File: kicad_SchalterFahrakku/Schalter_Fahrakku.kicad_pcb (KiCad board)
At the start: 2 copper layers, 15 parts, among them P1 V+_IN, P2 V-_IN, P3 V+_OUT, P4 V-_OUT, Q1 IRLML6344, Q2 IPD90P03

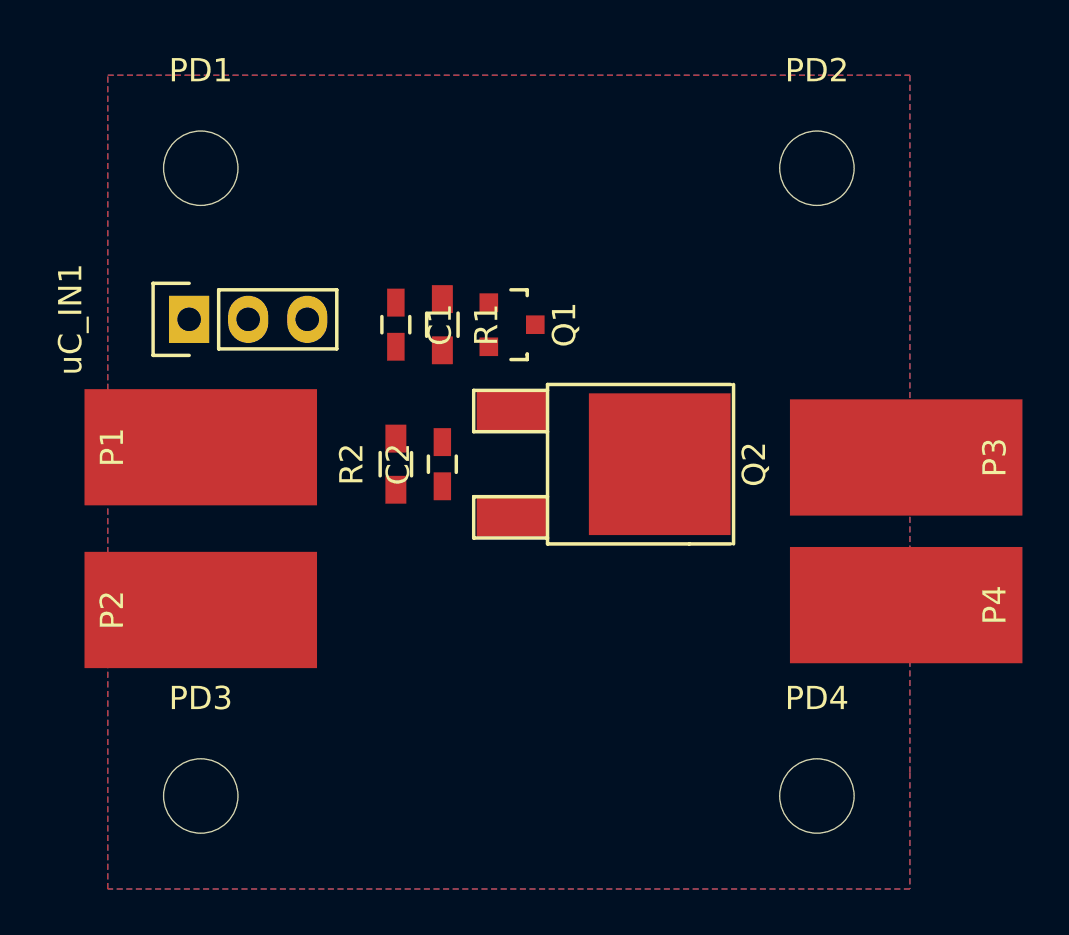
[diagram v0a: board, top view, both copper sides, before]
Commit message: - Neue anschlüsse in Schalterplatine eingefügt
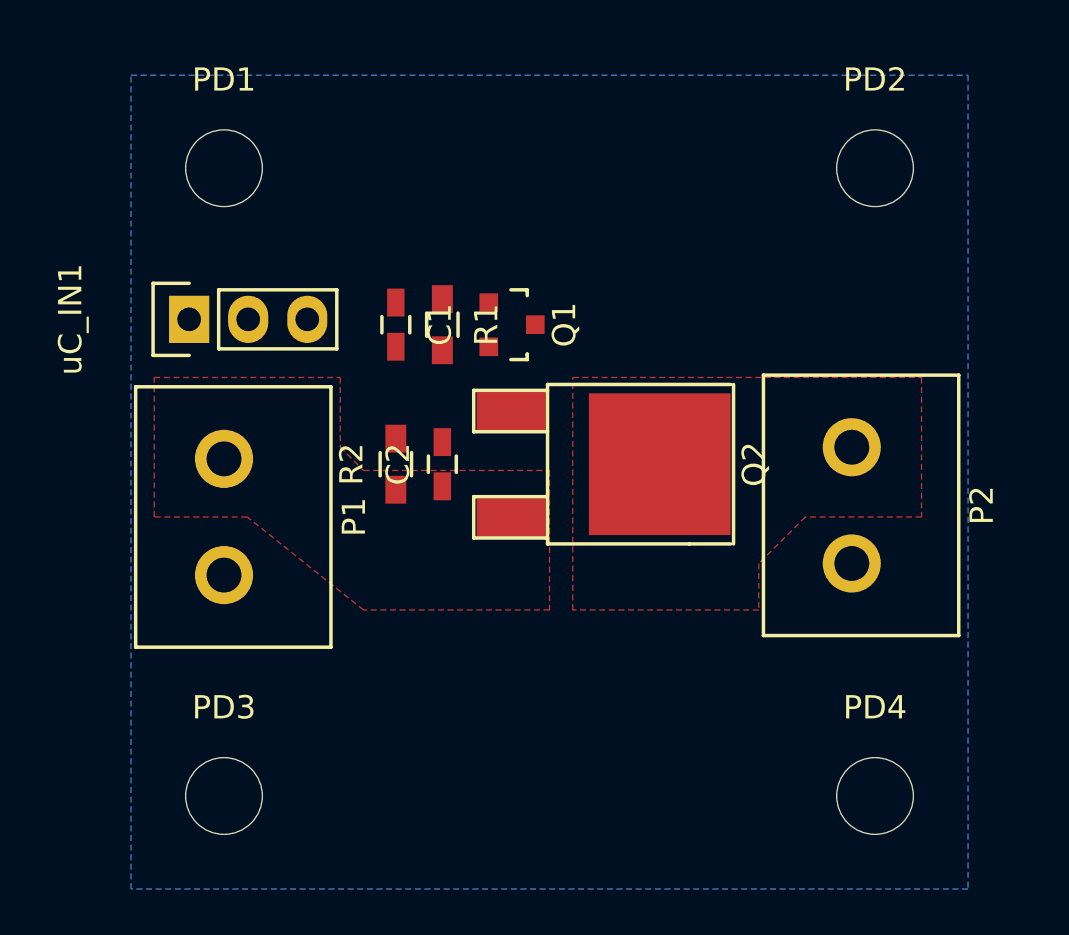
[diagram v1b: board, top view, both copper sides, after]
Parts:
- removed P3: V+_OUT, Wire_Pads:SolderWirePad_single_SMD_5x10mm
- removed P4: V-_OUT, Wire_Pads:SolderWirePad_single_SMD_5x10mm
- P1: value V+_IN -> V_IN; footprint Wire_Pads:SolderWirePad_single_SMD_5x10mm -> Custom:AKL_320-02
- P2: value V-_IN -> V_OUT; footprint Wire_Pads:SolderWirePad_single_SMD_5x10mm -> Custom:AKL_320-02
- PD1, PD2, PD3, PD4: footprint Mounting_Holes:MountingHole_3.2mm_M3 -> Custom:MountingHole_3.3mm_M3
- moved P2 28.9 mm to (178.0, 91.0), turned to 270 degrees
- moved PD2 2.50 mm to (179.0, 79.0)
- moved PD4 2.50 mm to (179.0, 106.0)
- moved P1 1.12 mm to (151.0, 91.5), turned to 270 degrees
- moved PD1 1.00 mm to (151.0, 79.0)
- moved PD3 1.00 mm to (151.0, 106.0)
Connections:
- P2 pad 1: GND -> Net-(P2-Pad1)
- Q2 pad 2: Net-(P3-Pad1) -> Net-(P2-Pad1)
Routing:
- added copper zone on F.Cu, net Net-(C2-Pad1)
- added copper zone on F.Cu, net Net-(P2-Pad1)
- removed copper zone on F.Cu, net GND

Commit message: - RC-Glieder an ADC hinzugefügt - Wannenstecker mit Spannungsversorgung an Op-Amps hinzugefügt - 0R Widerstände an Op-Amp Ausgängen hinzugefügt
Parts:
- moved P2 5.10 mm to (179.0, 96.0), turned to 90 degrees
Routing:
- added copper zone on F.Cu, net GND
- removed copper zone on F.Cu, net Net-(P2-Pad1)
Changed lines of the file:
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@@
     (links 16)
     (no_connects 16)
-    (area 143.275 74.075 184.375 110.775)
+    (area 143.275 74.075 184.575 110.775)
     (thickness 1.6)
     (drawings 4)
@@
   )
   (module Custom:AKL_320-02 (layer F.Cu)
-    (at 178 91 270)
-    (fp_text reference P2 (at 2.5 -5.6 270) (layer F.SilkS)
-      (effects (font (size 1 1) (thickness 0.15)))
-    )
-    (fp_text value V_OUT (at 2.5 4.8 270) (layer F.Fab)
+    (at 179 96 90)
+    (fp_text reference P2 (at 2.5 -5.6 90) (layer F.SilkS)
+      (effects (font (size 1 1) (thickness 0.15)))
+    )
+    (fp_text value V_OUT (at 2.5 4.8 90) (layer F.Fab)
       (effects (font (size 1 1) (thickness 0.15)))
     )
@@
     (fp_line (start -3.1 -4.6) (end 8.1 -4.6) (layer F.SilkS) (width 0.15))
     (fp_line (start -3.1 3.8) (end 8.1 3.8) (layer F.SilkS) (width 0.15))
-    (pad 2 thru_hole circle (at 5 0 270) (size 2.5 2.5) (drill 1.5) (layers *.Cu *.Mask F.SilkS)
-      (net 2 GND))
-    (pad 1 thru_hole circle (at 0 0 270) (size 2.5 2.5) (drill 1.5) (layers *.Cu *.Mask F.SilkS)
+    (pad 2 thru_hole circle (at 5 0 90) (size 2.5 2.5) (drill 1.5) (layers *.Cu *.Mask F.SilkS)
+      (net 2 GND))
+    (pad 1 thru_hole circle (at 0 0 90) (size 2.5 2.5) (drill 1.5) (layers *.Cu *.Mask F.SilkS)
       (net 5 "Net-(P2-Pad1)"))
   )
@@
   (gr_line (start 183 110) (end 183 75) (angle 90) (layer Margin) (width 0.2))
   (gr_line (start 147 110) (end 183 110) (angle 90) (layer Margin) (width 0.2))
-  (zone (net 3) (net_name "Net-(C2-Pad1)") (layer F.Cu) (hatch edge 0.508)
-    (connect_pads (clearance 0.508))
-    (min_thickness 0.254)
-    (fill yes (arc_segments 16) (thermal_gap 0.508) (thermal_bridge_width 0.508))
-    (polygon
-      (pts
-        (xy 156 91) (xy 157 92) (xy 165 92) (xy 165 98) (xy 157 98)
-        (xy 152 94) (xy 148 94) (xy 148 88) (xy 156 88) (xy 156 91)
-      )
-    )
-  )
-  (zone (net 5) (net_name "Net-(P2-Pad1)") (layer F.Cu) (hatch edge 0.508)
-    (connect_pads (clearance 0.508))
-    (min_thickness 0.254)
-    (fill yes (arc_segments 16) (thermal_gap 0.508) (thermal_bridge_width 0.508))
-    (polygon
-      (pts
-        (xy 181 94) (xy 176 94) (xy 174 96) (xy 174 98) (xy 166 98)
-        (xy 166 88) (xy 181 88) (xy 181 94)
-      )
-    )
-  )
   (zone (net 2) (net_name GND) (layer B.Cu) (hatch edge 0.508)
     (connect_pads (clearance 0.508))
@@
       )
     )
+  )
+  (zone (net 2) (net_name GND) (layer F.Cu) (hatch edge 0.508)
+    (connect_pads (clearance 0.508))
+    (min_thickness 0.254)
+    (fill (arc_segments 16) (thermal_gap 0.508) (thermal_bridge_width 0.508))
+    (polygon
+      (pts
+        (xy 183 110) (xy 147 110) (xy 147 75) (xy 183 75) (xy 183 110)
+      )
+    )
+    (polygon
+      (pts        (xy 165.75 87.5) (xy 165.75 91.5) (xy 156.75 91.5) (xy 154.75 89) (xy 148.5 89)
+        (xy 148.5 94) (xy 153.5 94) (xy 155.25 96) (xy 172.5 96) (xy 175 98.5)
+        (xy 181.5 98.5) (xy 181.5 93.5) (xy 176.5 93.5) (xy 174.25 91) (xy 174.25 87.5)
+        (xy 165.75 87.5)
+      )
+    )
+  )
+  (zone (net 3) (net_name "Net-(C2-Pad1)") (layer F.Cu) (hatch edge 0.508)
+    (connect_pads (clearance 0.508))
+    (min_thickness 0.254)
+    (fill (arc_segments 16) (thermal_gap 0.508) (thermal_bridge_width 0.508))
+    (polygon
+      (pts
+        (xy 156.5 92.5) (xy 165 92.5) (xy 165 95.25) (xy 155.75 95.25) (xy 154 93.25)
+        (xy 149.25 93.25) (xy 149.25 89.75) (xy 154.25 89.75)
+      )
+    )
+    (polygon
+      (pts        (xy 149.25 89.75)
+      )
+    )

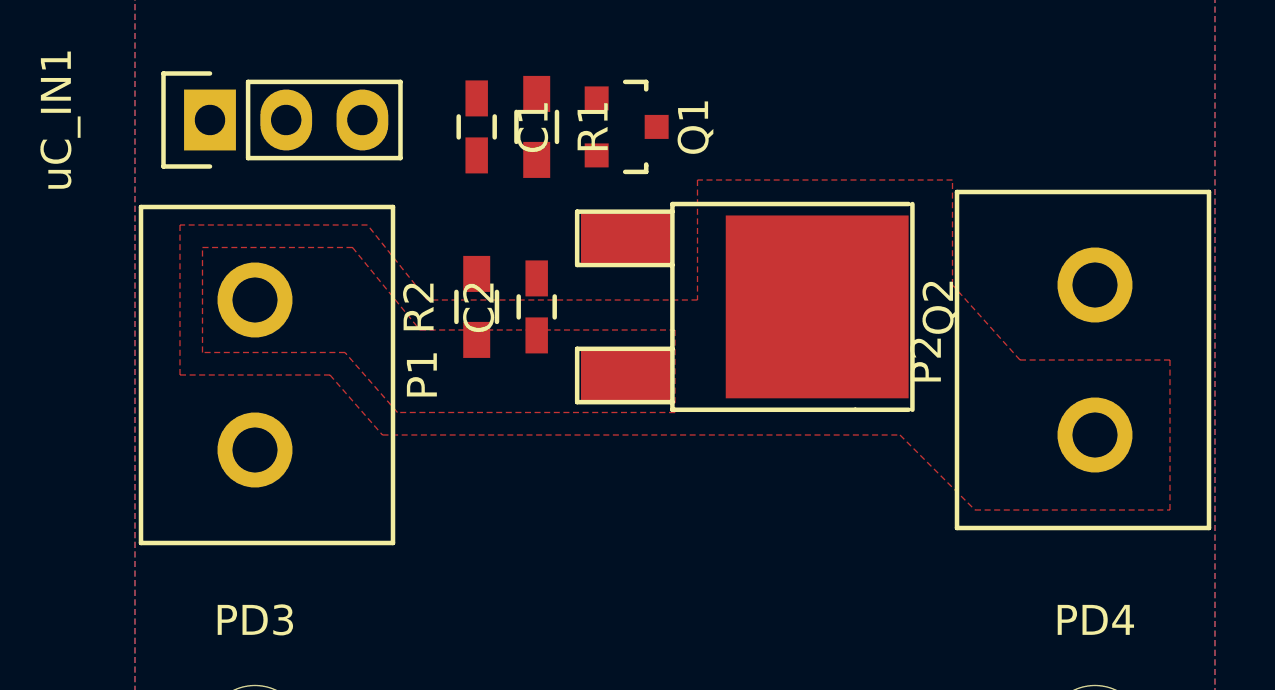
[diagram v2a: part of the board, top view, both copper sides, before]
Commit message: - Schaltplan uCSensorik finalisiert (1 pin an uC Frei geworden) - ERC wirft 8 Warnungen, keine Fehler
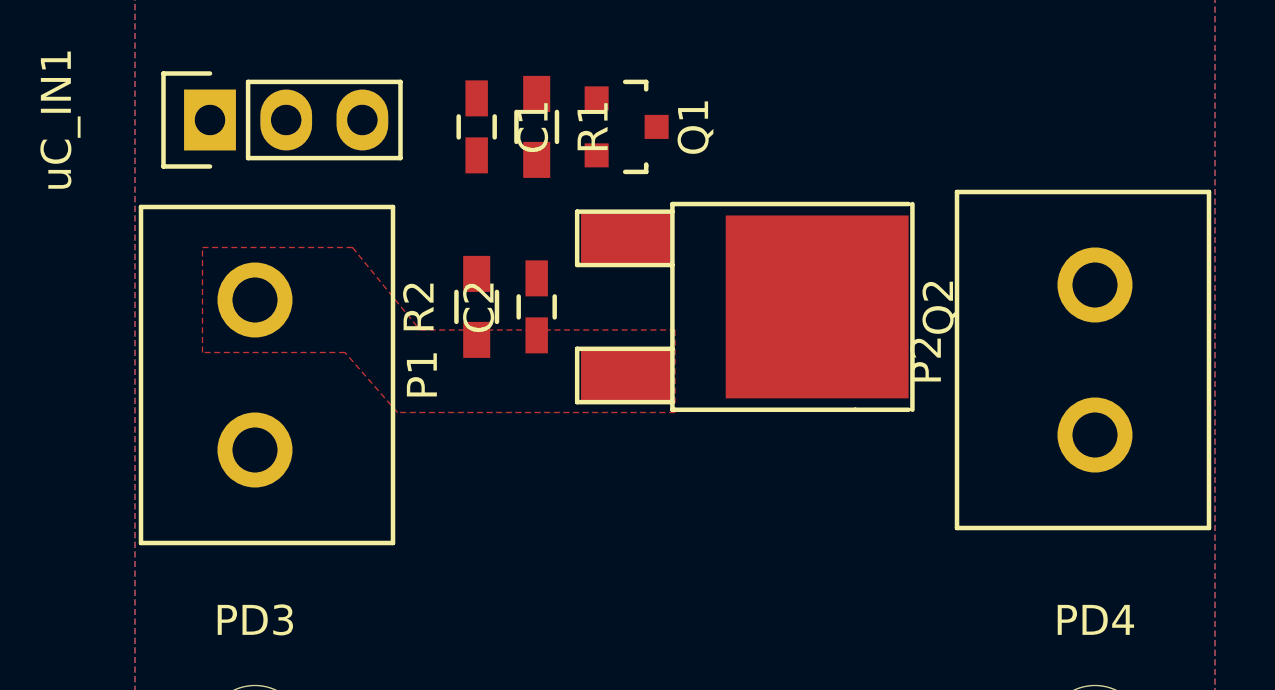
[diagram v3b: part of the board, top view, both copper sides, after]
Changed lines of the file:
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@@
   (general
     (links 16)
-    (no_connects 16)
-    (area 143.275 74.075 184.575 110.775)
+    (no_connects 8)
+    (area 143.275 74.075 184.775 110.775)
     (thickness 1.6)
     (drawings 4)
@@
     (connect_pads (clearance 0.508))
     (min_thickness 0.254)
-    (fill (arc_segments 16) (thermal_gap 0.508) (thermal_bridge_width 0.508))
+    (fill yes (arc_segments 16) (thermal_gap 0.508) (thermal_bridge_width 0.508))
     (polygon
       (pts
@@
     (connect_pads (clearance 0.508))
     (min_thickness 0.254)
-    (fill (arc_segments 16) (thermal_gap 0.508) (thermal_bridge_width 0.508))
+    (fill yes (arc_segments 16) (thermal_gap 0.508) (thermal_bridge_width 0.508))
     (polygon
       (pts
@@
       )
     )
-    (polygon
-      (pts        (xy 165.75 87.5) (xy 165.75 91.5) (xy 156.75 91.5) (xy 154.75 89) (xy 148.5 89)
-        (xy 148.5 94) (xy 153.5 94) (xy 155.25 96) (xy 172.5 96) (xy 175 98.5)
-        (xy 181.5 98.5) (xy 181.5 93.5) (xy 176.5 93.5) (xy 174.25 91) (xy 174.25 87.5)
-        (xy 165.75 87.5)
-      )
-    )
   )
   (zone (net 3) (net_name "Net-(C2-Pad1)") (layer F.Cu) (hatch edge 0.508)
+    (priority 1)
     (connect_pads (clearance 0.508))
     (min_thickness 0.254)
-    (fill (arc_segments 16) (thermal_gap 0.508) (thermal_bridge_width 0.508))
+    (fill yes (arc_segments 16) (thermal_gap 0.508) (thermal_bridge_width 0.508))
     (polygon
       (pts

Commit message: - Layout Grob sortiert - Fehler an CAR-ID DIP behoben(Pin Zuordnung Fehlerhaft) - Fehler an GNDD behoben (GNDA und GNDD vertauscht an TEN30)
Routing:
- removed copper zone on F.Cu, net Net-(C2-Pad1)
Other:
- net class Default: via_drill 0.4 -> 0.2
- rule via_min_drill: 0.3 -> 0.2
- rule via_min_size: 0.4 -> 0.6
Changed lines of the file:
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@@
   (setup
     (last_trace_width 0.25)
+    (user_trace_width 0.2)
+    (user_trace_width 0.25)
+    (user_trace_width 0.3)
+    (user_trace_width 0.5)
+    (user_trace_width 0.8)
+    (user_trace_width 1)
+    (user_trace_width 2)
     (trace_clearance 0.2)
     (zone_clearance 0.508)
@@
     (edge_width 0.15)
     (via_size 0.6)
-    (via_drill 0.4)
-    (via_min_size 0.4)
-    (via_min_drill 0.3)
+    (via_drill 0.2)
+    (via_min_size 0.6)
+    (via_min_drill 0.2)
+    (user_via 0.6 0.2)
+    (user_via 1.2 0.8)
+    (user_via 1.4 1)
+    (user_via 9 0.5)
     (uvia_size 0.3)
     (uvia_drill 0.1)
@@
     (trace_width 0.25)
     (via_dia 0.6)
-    (via_drill 0.4)
+    (via_drill 0.2)
     (uvia_dia 0.3)
     (uvia_drill 0.1)
@@
       )
     )
-  )
-  (zone (net 3) (net_name "Net-(C2-Pad1)") (layer F.Cu) (hatch edge 0.508)
-    (priority 1)
-    (connect_pads (clearance 0.508))
-    (min_thickness 0.254)
-    (fill yes (arc_segments 16) (thermal_gap 0.508) (thermal_bridge_width 0.508))
-    (polygon
-      (pts
-        (xy 156.5 92.5) (xy 165 92.5) (xy 165 95.25) (xy 155.75 95.25) (xy 154 93.25)
-        (xy 149.25 93.25) (xy 149.25 89.75) (xy 154.25 89.75)
-      )
-    )
-    (polygon
-      (pts        (xy 149.25 89.75)
-      )
-    )

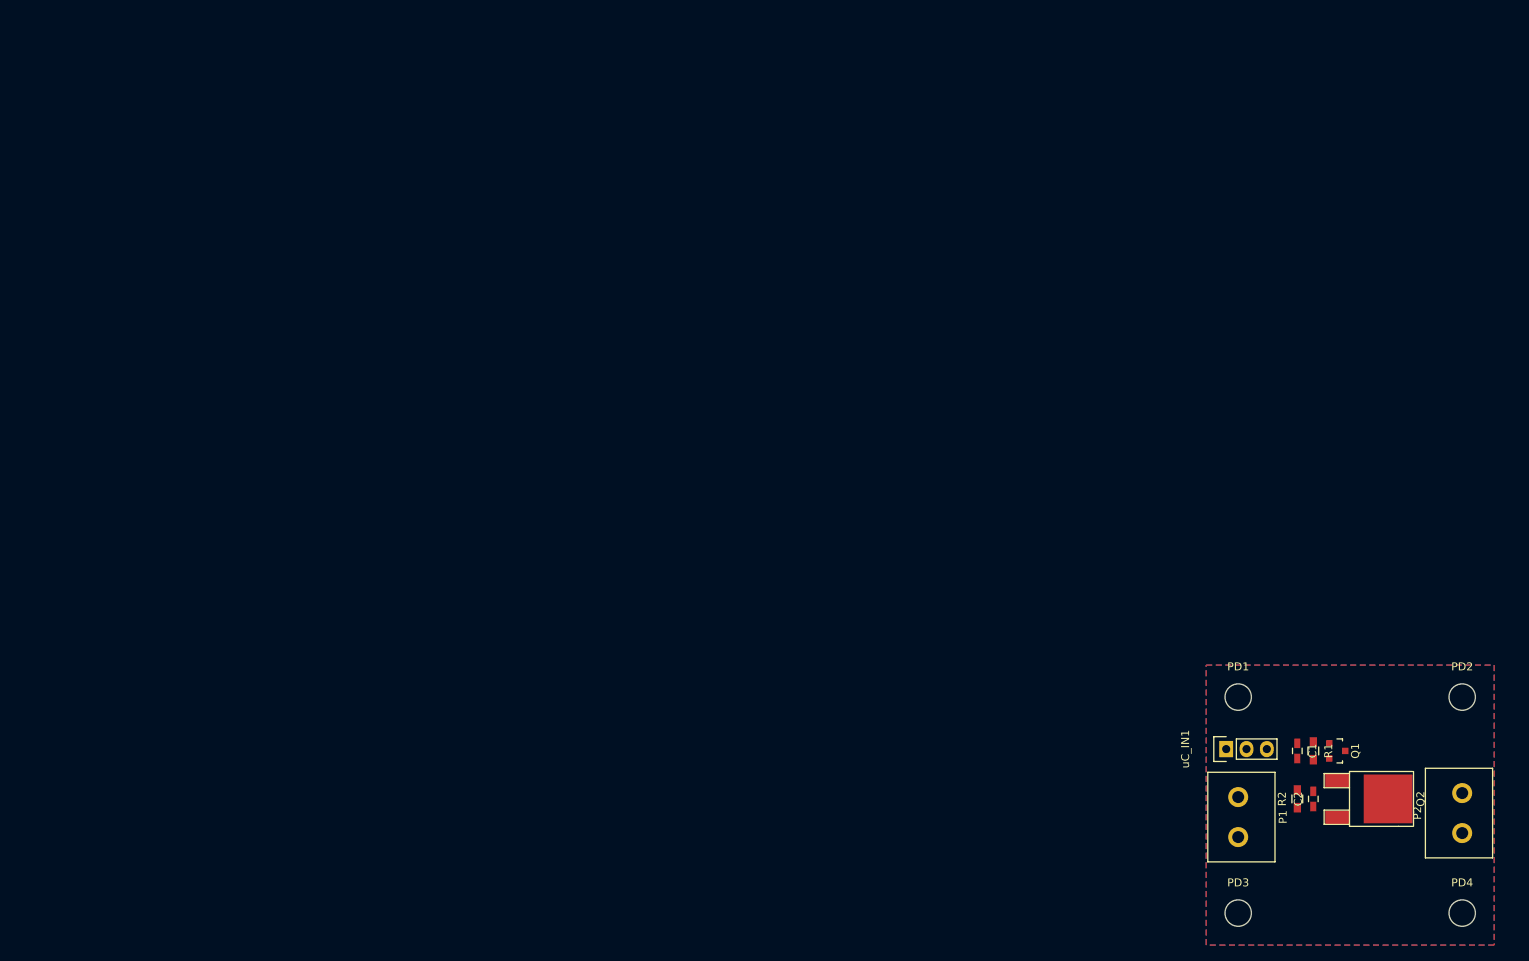
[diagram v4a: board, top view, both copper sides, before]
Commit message: - RC-Glieder im Schaltplan hinzugefügt - LED4 Hinzugefügt
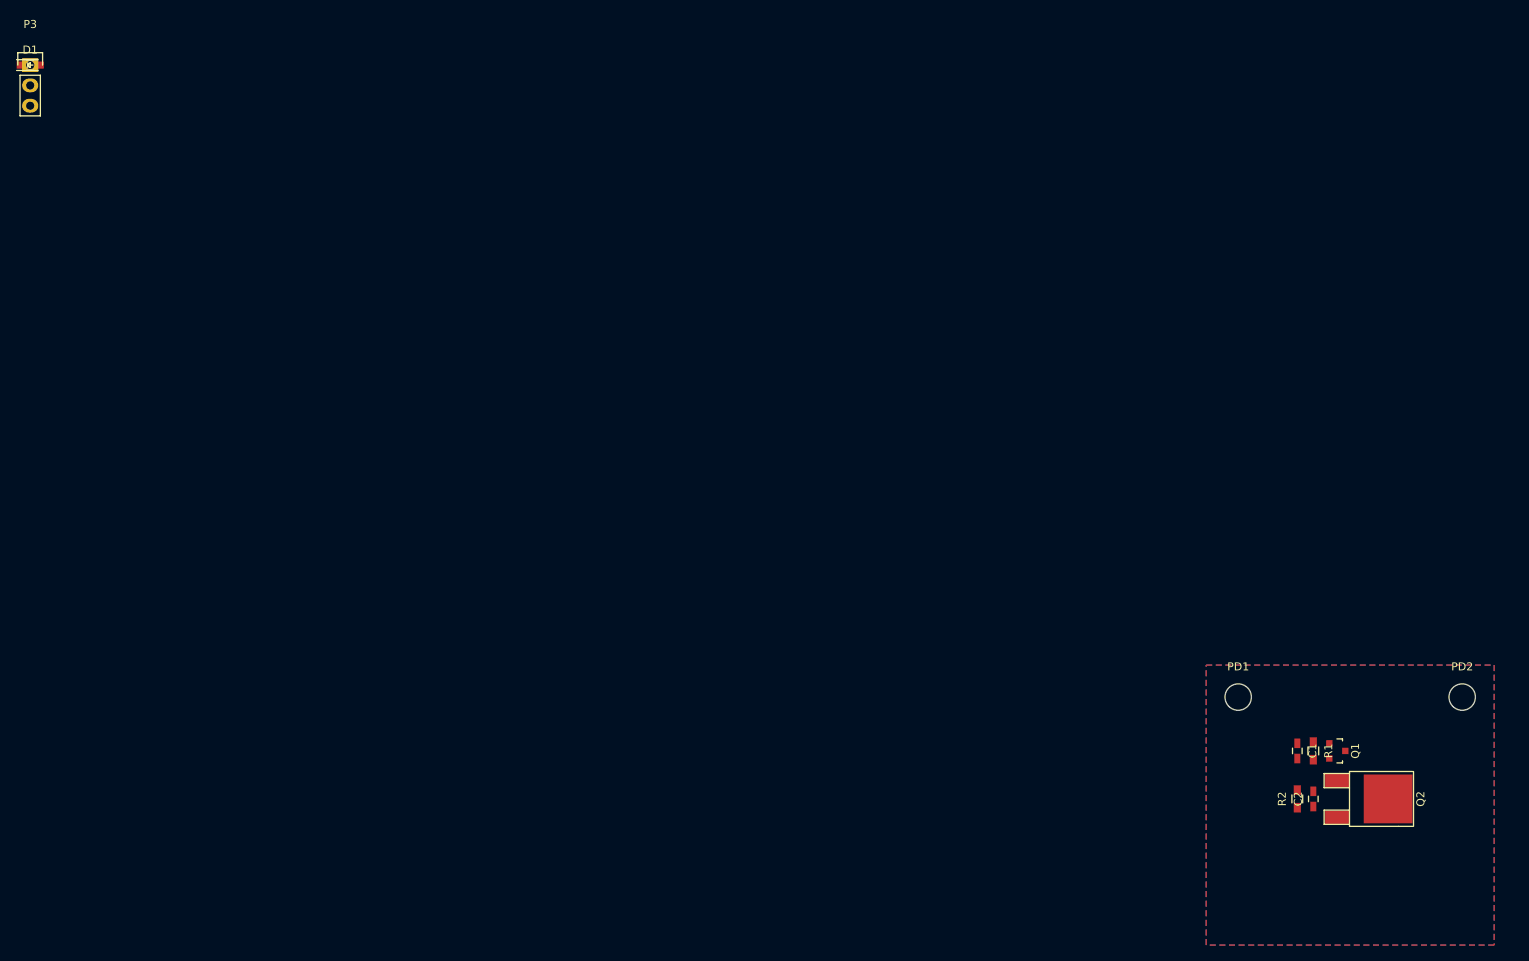
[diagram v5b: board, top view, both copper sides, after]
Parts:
- removed P1: V_IN, Custom:AKL_320-02
- removed P2: V_OUT, Custom:AKL_320-02
- removed PD3, PD4: Hole, Custom:MountingHole_3.3mm_M3
- removed uC_IN1: SIL 3, Pin_Headers:Pin_Header_Straight_1x03
- added D1: LED, Custom:LED_0603_HandSoldering, F.Cu at (0.00, 0.00)
- added P3: uC_IN, Pin_Headers:Pin_Header_Straight_1x03, F.Cu at (0.00, 0.00)
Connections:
- Q2 pad 2: Net-(P2-Pad1) -> (no net)
